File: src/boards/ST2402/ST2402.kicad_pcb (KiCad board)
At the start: 2 copper layers, 228.6 x 86.4 mm, 94 parts, among them J1 Conn_02x19_Odd_Even, J11 Conn_02x02_Top_Bottom, J12 Conn_02x02_Top_Bottom, J13 BNC, J14 Screw_Terminal_01x01, J15 Screw_Terminal_01x01, J16 Screw_Terminal_01x01, J17 Screw_Terminal_01x01, J18 Screw_Terminal_01x01, J19 BNC, J2 Conn_02x19_Odd_Even, J21 Conn_02x03_Top_Bottom, J22 Conn_02x03_Top_Bottom, J3 Conn_01x08, J4 Conn_01x08, J5 Conn_01x06, J6 Conn_01x10, J7 Conn_01x02, J8 Conn_01x02, J9 Screw_Terminal_01x02, Q1 STB100N10F7, Q2 STB100N10F7, U1 L6494LD

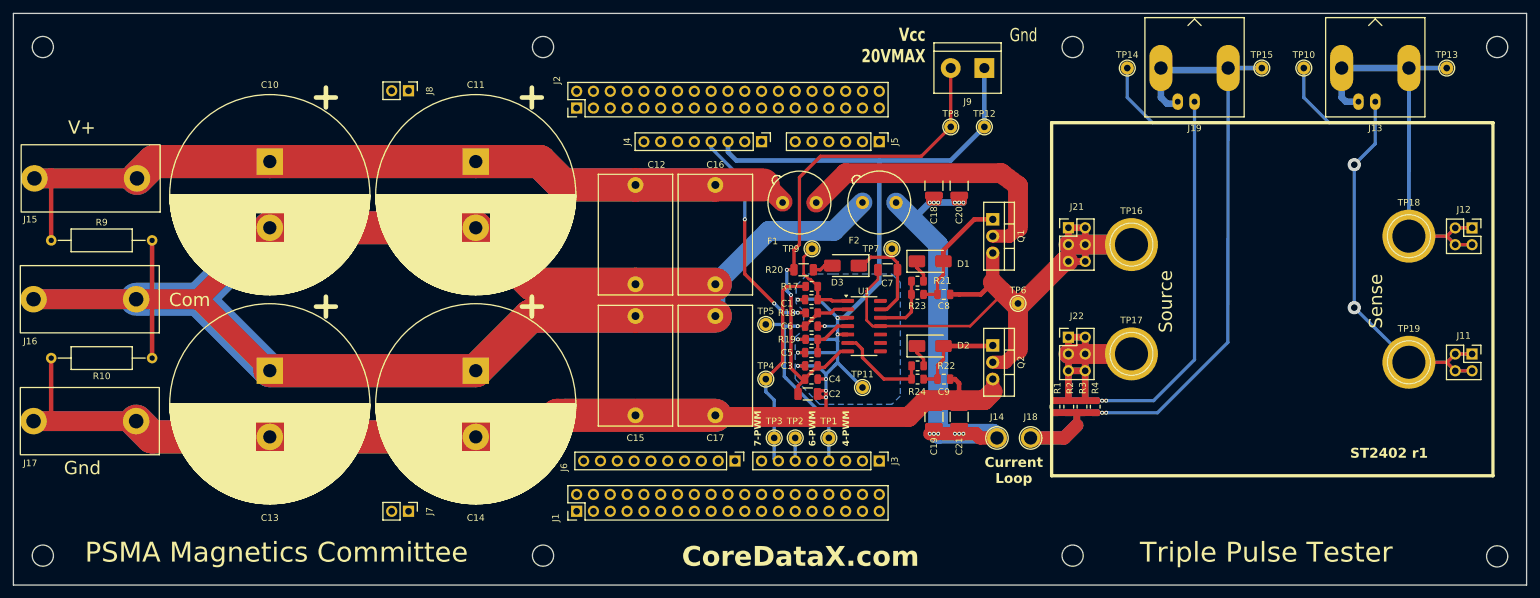
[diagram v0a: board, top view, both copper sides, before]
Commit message: Updated pcb files
Added r2 and r3 gerbers and updated KiCad file (r3)
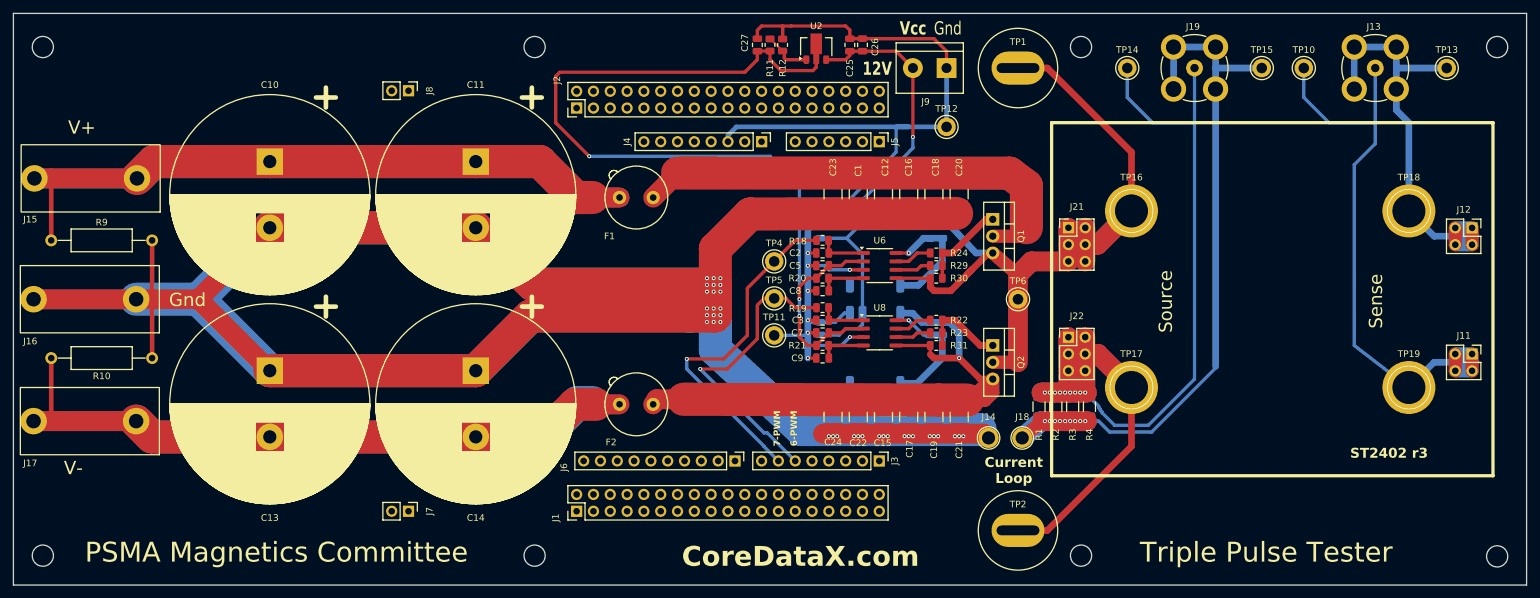
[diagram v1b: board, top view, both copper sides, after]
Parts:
- removed D1, D2: 30V,2A, Diode_SMD:D_SMA
- removed D3: D, Diode_SMD:D_SMA
- removed R17: 1k, Resistor_SMD:R_0805_2012Metric
- removed TP3, TP8: TestPoint, TestPoint:TestPoint_THTPad_D2.0mm_Drill1.0mm
- removed TP7: ORG, TestPoint:TestPoint_THTPad_D2.0mm_Drill1.0mm
- removed TP9: WHT, TestPoint:TestPoint_THTPad_D2.0mm_Drill1.0mm
- added C22: 10uF, Capacitor_SMD:C_1210_3225Metric, F.Cu at (160.0, 114.9)
- added C23: 10uF, Capacitor_SMD:C_1210_3225Metric, F.Cu at (156.2, 81.3)
- added C24: 10uF, Capacitor_SMD:C_1210_3225Metric, F.Cu at (156.2, 114.9)
- added C25: 100nF, Capacitor_SMD:C_0805_2012Metric, F.Cu at (158.8, 58.7)
- added C26: 10uF, Capacitor_SMD:C_0805_2012Metric, F.Cu at (160.7, 58.7)
- added C27: 1uF 25V, Capacitor_SMD:C_0805_2012Metric, F.Cu at (144.8, 58.7)
- added C34: 10uF 25V, Capacitor_SMD:C_0805_2012Metric, B.Cu at (170.8, 87.0)
- added C35: 10uF, Capacitor_SMD:C_0805_2012Metric, B.Cu at (170.8, 101.6)
- added C36: 1uF 25V, Capacitor_SMD:C_0805_2012Metric, B.Cu at (172.7, 87.0)
- added C37: 1uF, Capacitor_SMD:C_0805_2012Metric, B.Cu at (172.7, 101.6)
- added R11: 470R, Resistor_SMD:R_0805_2012Metric, F.Cu at (146.7, 58.7)
- added R12: 1k88, Resistor_SMD:R_0805_2012Metric, F.Cu at (148.6, 58.7)
- added R29: 2R, Resistor_SMD:R_0805_2012Metric, F.Cu at (171.8, 92.1)
- added R30: 100k, Resistor_SMD:R_0805_2012Metric, F.Cu at (171.8, 94.0)
- added R31: 100k, Resistor_SMD:R_0805_2012Metric, F.Cu at (171.8, 104.1)
- added U2: LM317L_SOT-89, Package_TO_SOT_SMD:SOT-89-3, F.Cu at (153.7, 59.0)
- added U6: ~, Package_SO:SOIC-8_3.9x4.9mm_P1.27mm, F.Cu at (163.3, 92.1)
- added U7: ~, GS_Library:5_pin_single_smd, B.Cu at (162.6, 104.6)
- added U8: ~, Package_SO:SOIC-8_3.9x4.9mm_P1.27mm, F.Cu at (163.3, 102.2)
- C1: value 33pF/25V -> 10uF; footprint Capacitor_SMD:C_0805_2012Metric -> Capacitor_SMD:C_1210_3225Metric
- C12, C15, C16, C17: value 4.7uF -> 10uF; footprint Capacitor_THT:C_Rect_L18.0mm_W11.0mm_P15.00mm_FKS3_FKP3 -> Capacitor_SMD:C_1210_3225Metric
- C2: value 10uF 50V -> 100nF; footprint Capacitor_SMD:C_1206_3216Metric -> Capacitor_SMD:C_0805_2012Metric
- C20, C21: value 10uF 50V -> 10uF
- C3: value 220nF 50V -> 100nF
- C4: value 220nF 50V -> 10uF 25V; moved to B.Cu
- C5: value 220nF/50V -> 100nF
- C6: value 33pF/25V -> 10uF; moved to B.Cu
- C7: value 2.2uF -> 100nF; footprint Capacitor_SMD:C_1206_3216Metric -> Capacitor_SMD:C_0805_2012Metric
- C8, C9: value C -> 100nF
- J13, J19: footprint Connector_Coaxial:BNC_Amphenol_B6252HB-NPP3G-50_Horizontal -> Connector_Coaxial:BNC_TEConnectivity_1478204_Vertical
- R1, R2, R3, R4, R5, R6, R7, R8: footprint Resistor_SMD:R_0805_2012Metric -> Resistor_SMD:R_1206_3216Metric
- R18: value 43k -> 100R
- R19: value R -> 100R
- R20: value 10R -> 10k; footprint Resistor_SMD:R_1206_3216Metric -> Resistor_SMD:R_0805_2012Metric
- R21: value R -> 10k
- R22: value R -> 10R
- R23: value 10R -> 2R
- TP1, TP2: footprint TestPoint:TestPoint_THTPad_D2.0mm_Drill1.0mm -> TestPoint:TestPoint_Plated_Hole_D5.0mm
- TP10, TP11, TP12, TP13, TP14, TP15, TP4, TP5, TP6: footprint TestPoint:TestPoint_THTPad_D2.0mm_Drill1.0mm -> TestPoint:TestPoint_Keystone_5010-5014_Multipurpose
- U1: value L6494LD -> ~; footprint Package_SO:SO-14_3.9x8.65mm_P1.27mm -> GS_Library:5_pin_single_smd; moved to B.Cu
- moved TP1 62.8 mm to (184.2, 62.2)
- moved F2 47.7 mm to (129.0, 113.0)
- moved C15 40.4 mm to (163.8, 114.9), turned to 90 degrees
- moved C12 37.5 mm to (163.8, 81.3)
- moved TP2 36.4 mm to (184.2, 132.1)
- moved C17 32.9 mm to (167.6, 114.9), turned to 90 degrees
- moved C16 29.2 mm to (167.6, 81.3)
- moved F1 24.6 mm to (129.0, 81.8)
- moved C2 21.4 mm to (154.6, 90.2), turned to 180 degrees
- moved R24 19.3 mm to (171.8, 90.2)
- moved C9 18.6 mm to (154.6, 106.0), turned to 180 degrees
- moved C8 18.3 mm to (154.6, 95.9), turned to 180 degrees
- moved TP4 17.8 mm to (147.3, 91.4)
- moved C1 17.4 mm to (160.0, 81.3), turned to -90 degrees
- moved R21 17.3 mm to (154.6, 104.1)
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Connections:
- C1 pad 1: Net-(U1-IN) -> Net-(Q1-D)
- C1 pad 2: GND -> FIX_B
- C10 pad 2: Net-(J16-Pin_1) -> FIX_B
- C11 pad 2: Net-(J16-Pin_1) -> FIX_B
- C12 pad 1: Net-(J15-Pin_1) -> Net-(Q1-D)
- C12 pad 2: Net-(J16-Pin_1) -> FIX_B
- C13 pad 1: Net-(J16-Pin_1) -> FIX_B
- C13 pad 2: GND -> Net-(J17-Pin_1)
- C14 pad 1: Net-(J16-Pin_1) -> FIX_B
- C14 pad 2: GND -> Net-(J17-Pin_1)
- C15 pad 1: Net-(J16-Pin_1) -> FIX_B
- C15 pad 2: GND -> Net-(Q2-S)
- C16 pad 1: Net-(J15-Pin_1) -> Net-(Q1-D)
- C16 pad 2: Net-(J16-Pin_1) -> FIX_B
- C17 pad 1: Net-(J16-Pin_1) -> FIX_B
- C17 pad 2: GND -> Net-(Q2-S)
- C19 pad 2: GND -> Net-(Q2-S)
- C2 pad 1: Net-(J9-Pin_2) -> Net-(U6-VI)
- C21 pad 2: GND -> Net-(Q2-S)
- C3 pad 1: Net-(J9-Pin_2) -> Net-(U8-VI)
- C4 pad 1: Net-(J9-Pin_2) -> +12V
- C5 pad 1: Net-(U1-DT) -> +5V
- C6 pad 1: SD -> +12V
- C7 pad 1: Net-(D3-K) -> +5V
- C7 pad 2: FIX_A -> GND
- C8 pad 1: Net-(D1-A) -> Net-(U6-EN)
- C8 pad 2: FIX_A -> GND
- C9 pad 1: Net-(D2-A) -> Net-(U8-EN)
- F2 pad 1: FIX_B -> Net-(Q2-S)
- F2 pad 2: Net-(J16-Pin_1) -> Net-(J17-Pin_1)
- J16 pad 1: Net-(J16-Pin_1) -> FIX_B
- J17 pad 1: GND -> Net-(J17-Pin_1)
- J3 pad 4: SD -> unconnected-(J3-Pin_4-Pad4)
- J3 pad 6: Net-(J3-Pin_6) -> PWM_L
- J3 pad 7: PWM -> PWM_U
- J9 pad 2: Net-(J9-Pin_2) -> +12V
- Q1 pad 1: Net-(D1-A) -> Net-(Q1-G)
- Q2 pad 1: Net-(D2-A) -> Net-(Q2-G)
- Q2 pad 3: GND -> Net-(Q2-S)
- R10 pad 1: Net-(J16-Pin_1) -> FIX_B
- R10 pad 2: GND -> Net-(J17-Pin_1)
- R18 pad 1: 5V -> PWM_U
- R18 pad 2: SD -> Net-(U6-VI)
- R19 pad 1: Net-(U1-DT) -> PWM_L
- R19 pad 2: GND -> Net-(U8-VI)
- R20 pad 1: Net-(J9-Pin_2) -> +5V
- R20 pad 2: Net-(D3-A) -> Net-(U6-EN)
- R21 pad 1: Net-(U1-HVG) -> +5V
- R21 pad 2: Net-(D1-K) -> Net-(U8-EN)
- R22 pad 2: Net-(U1-LVG) -> Net-(Q2-G)
- R23 pad 1: Net-(U1-HVG) -> Net-(U8-VO-)
- R23 pad 2: Net-(D1-A) -> Net-(Q2-G)
- R24 pad 1: Net-(U1-LVG) -> Net-(U6-VO+)
- R24 pad 2: Net-(D2-A) -> Net-(Q1-G)
- R9 pad 2: Net-(J16-Pin_1) -> FIX_B
- TP1 pad 1: SD -> FIX_A
- TP2 pad 1: Net-(J3-Pin_6) -> Net-(J19-In)
- TP4 pad 1: PWM -> PWM_U
- TP5 pad 1: SD -> PWM_L
- U1 pad 1: Net-(U1-IN) -> GND
- U1 pad 2: SD -> +12V
- U1 pad 4: Net-(U1-DT) -> FIX_A
- U1 pad 5: GND -> Net-(U1-+Vout)
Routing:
- net FIX_B: track 72.6 -> 547.9 mm, vias 12 -> 36
- net Net-(J16-Pin_1): track 445.6 -> 0.00 mm
- net GND: track 411.0 -> 162.0 mm, vias 10 -> 8
- net Net-(J17-Pin_1): track 0.00 -> 192.9 mm
- net +5V: track 0.00 -> 140.6 mm, vias 0 -> 3
- net Net-(Q2-S): track 0.00 -> 92.6 mm, vias 0 -> 1
- net Net-(J9-Pin_2): track 78.4 -> 0.00 mm, vias 2 -> 0
- net +12V: track 0.00 -> 69.8 mm, vias 0 -> 1
- net PWM_U: track 0.00 -> 52.3 mm, vias 0 -> 1
- net PWM_L: track 0.00 -> 45.6 mm, vias 0 -> 1
- net Net-(J15-Pin_1): track 231.0 -> 192.7 mm
- net FIX_A: track 119.2 -> 156.5 mm
- net SD: track 36.8 -> 0.00 mm, vias 1 -> 0
- net Net-(J19-In): track 152.9 -> 189.5 mm, vias 2 -> 9
- net 5V: track 33.7 -> 0.00 mm, vias 3 -> 0
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- removed copper zone on B.Cu, net GND
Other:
- board text added: "12V"
- board text added: "ST2402 r3"
- board text added: "V-"
- board text added: "Vcc"
- board text removed: "4-PWM"
- board text removed: "Com"
- board text removed: "ST2402 r1"
- board text removed: "Vcc 20VMAX"
